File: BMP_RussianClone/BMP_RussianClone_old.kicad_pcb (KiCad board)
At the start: 2 copper layers, 42.1 x 116 mm, 57 parts, among them J1 BARREL_JACK, Q1 MMBT3904, Q2 MMBT3904, Q3 MMBT3904, Q4 MMBT3904

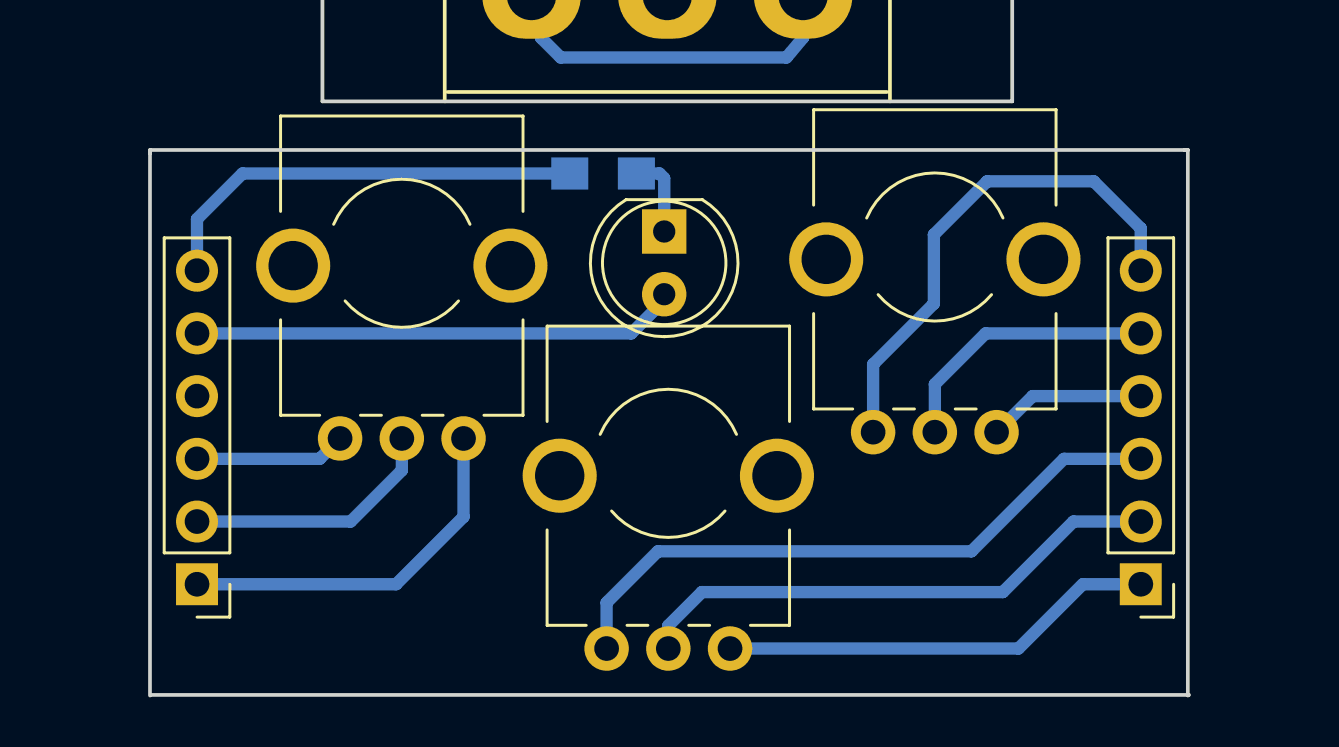
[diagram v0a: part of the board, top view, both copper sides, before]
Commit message: Moved sockets closer to  vertical edges
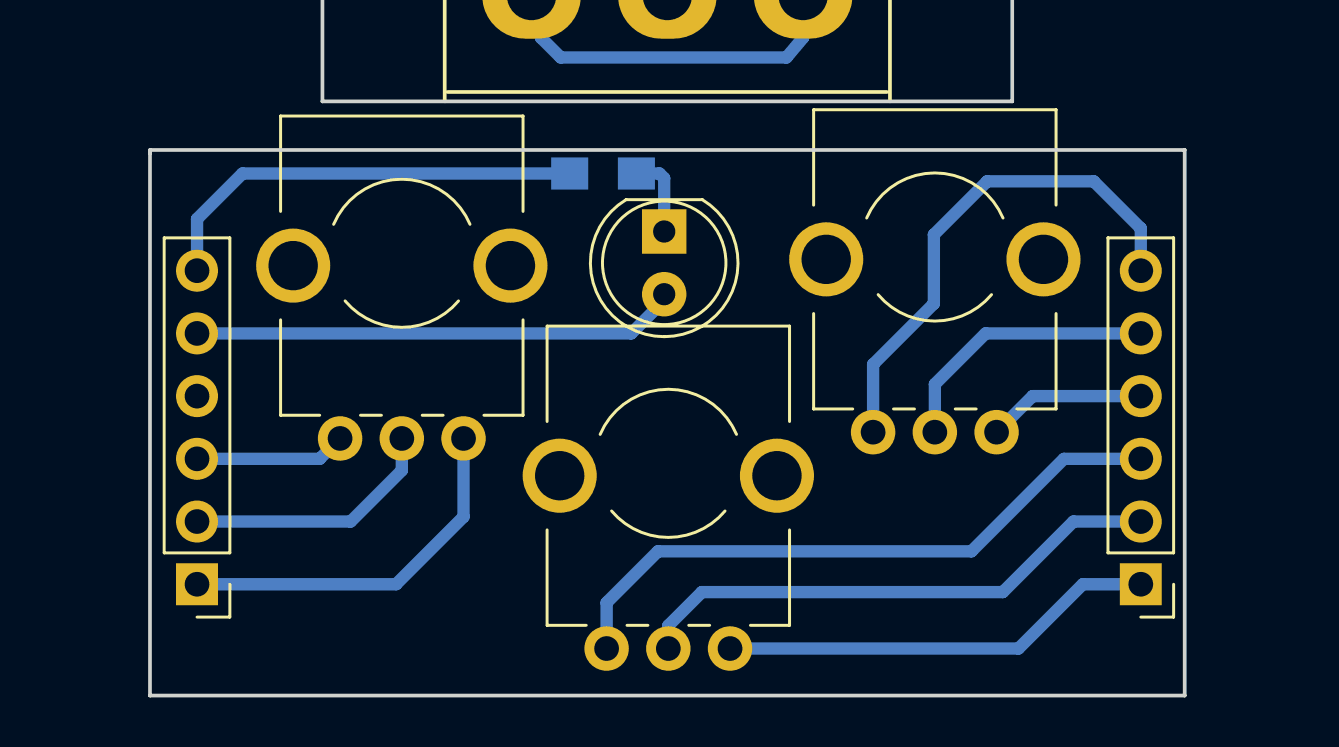
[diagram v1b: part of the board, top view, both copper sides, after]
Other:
- board size 42.1 x 116 mm -> 41.9 x 116 mm
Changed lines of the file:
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@@
     (links 96)
     (no_connects 0)
-    (area 44.936999 65.5512 117.247571 219.975501)
+    (area 54.026999 103.810999 96.264801 219.975501)
     (thickness 1.6)
-    (drawings 19)
+    (drawings 18)
     (tracks 487)
     (zones 0)
@@
     )
   )
+  (gr_line (start 96.012 197.8025) (end 54.102 197.8025) (angle 90) (layer Edge.Cuts) (width 0.15))
+  (gr_line (start 96.012 219.9005) (end 96.012 197.8025) (angle 90) (layer Edge.Cuts) (width 0.15))
+  (gr_line (start 54.102 219.9005) (end 96.012 219.9005) (angle 90) (layer Edge.Cuts) (width 0.15))
   (gr_line (start 96.012 188.849) (end 96.012 110.871) (angle 90) (layer Edge.Cuts) (width 0.15))
   (gr_line (start 61.087 195.834) (end 89.027 195.834) (angle 90) (layer Edge.Cuts) (width 0.15))
@@
   (gr_line (start 54.102 110.871) (end 54.102 188.849) (angle 90) (layer Edge.Cuts) (width 0.15))
   (gr_line (start 89.027 103.886) (end 61.087 103.886) (angle 90) (layer Edge.Cuts) (width 0.15))
-  (gr_line (start 96.139 197.8025) (end 54.102 197.8025) (angle 90) (layer Edge.Cuts) (width 0.15))
-  (gr_line (start 96.139 197.8025) (end 96.012 197.8025) (angle 90) (layer Edge.Cuts) (width 0.15))
-  (gr_line (start 96.139 219.9005) (end 96.139 197.8025) (angle 90) (layer Edge.Cuts) (width 0.15))
   (gr_line (start 54.102 219.9005) (end 54.102 197.9295) (angle 90) (layer Edge.Cuts) (width 0.15))
   (gr_line (start 54.102 197.8025) (end 54.102 197.9295) (angle 90) (layer Edge.Cuts) (width 0.15))
-  (gr_line (start 54.1782 219.8751) (end 96.1898 219.8751) (angle 90) (layer Edge.Cuts) (width 0.15))
   (gr_line (start 61.087 110.871) (end 54.102 110.871) (angle 90) (layer Edge.Cuts) (width 0.15))
   (gr_line (start 61.087 103.886) (end 61.087 110.871) (angle 90) (layer Edge.Cuts) (width 0.15))
